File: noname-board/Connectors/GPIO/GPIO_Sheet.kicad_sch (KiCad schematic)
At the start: 1 part, among them J1 GPIO_CONNECTOR

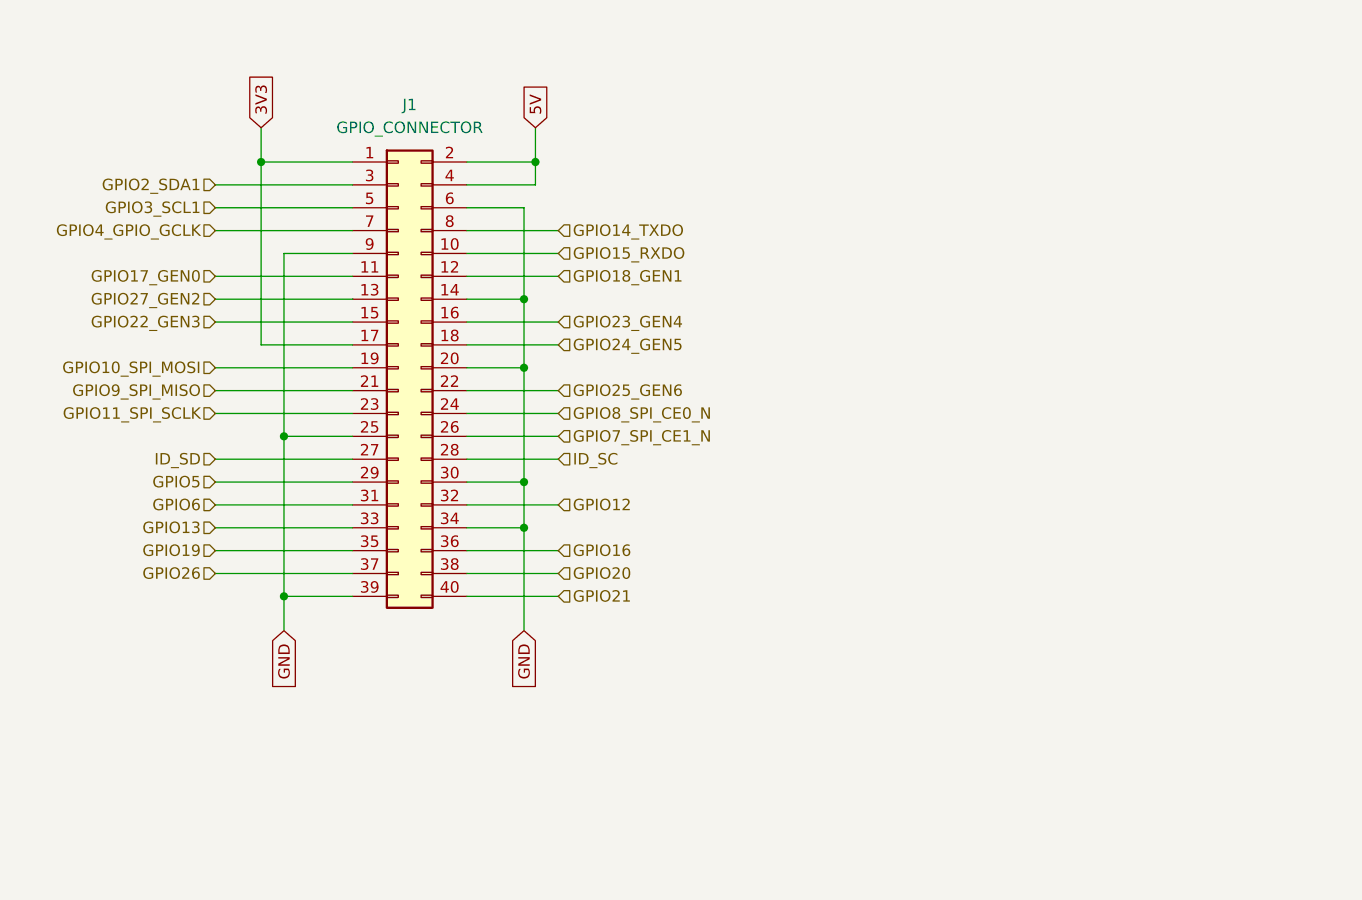
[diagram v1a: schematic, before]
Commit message: GPIO, USBC
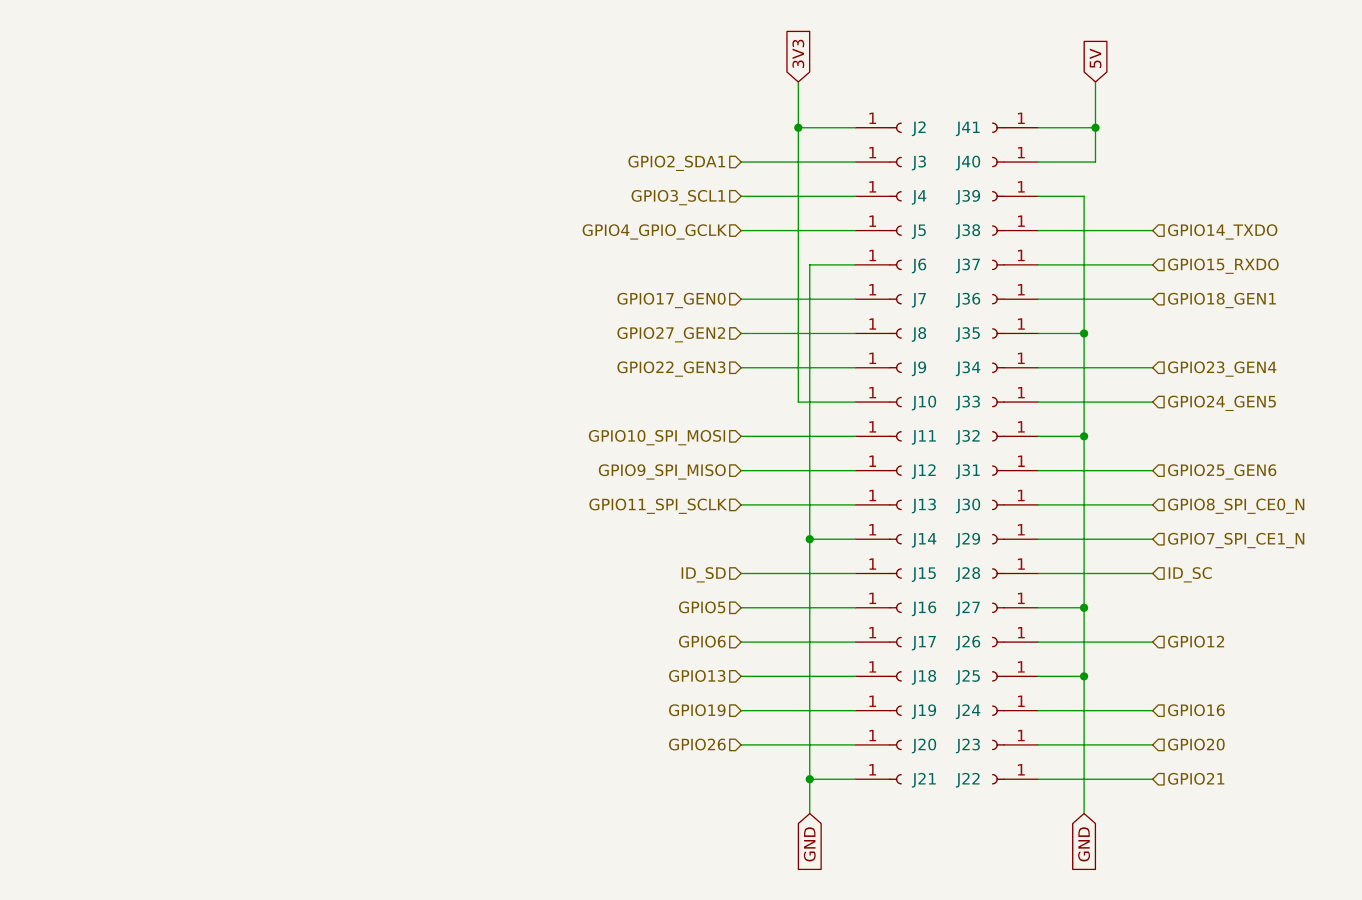
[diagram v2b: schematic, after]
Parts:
- removed J1: GPIO_CONNECTOR, symbol Connector_Generic:Conn_02x20_Odd_Even
- added J10, J11, J12, J13, J14, J15, J16, J17, J18, J19, J2, J20, J21, J22, J23, J24, J25, J26, J27, J28, J29, J3, J30, J31, J32, J33, J34, J35, J36, J37, J38, J39, J4, J40, J41, J5, J6, J7, J8, J9: Conn_01x01_Socket, Connector_PinSocket_2.00mm:PinSocket_1x01_P2.00mm_Vertical, symbol Connector:Conn_01x01_Socket
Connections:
- net 3V3: now also J10.1 (Pin_1), J2.1 (Pin_1)
- net 5V: now also J40.1 (Pin_1), J41.1 (Pin_1)
- net GND: now also J14.1 (Pin_1), J21.1 (Pin_1), J25.1 (Pin_1), J27.1 (Pin_1), J32.1 (Pin_1), J35.1 (Pin_1), J39.1 (Pin_1), J6.1 (Pin_1)
- net GPIO10_SPI_MOSI: now also J11.1 (Pin_1)
- net GPIO11_SPI_SCLK: now also J13.1 (Pin_1)
- net GPIO12: now also J26.1 (Pin_1)
- net GPIO13: now also J18.1 (Pin_1)
- net GPIO14_TXDO: now also J38.1 (Pin_1)
- net GPIO15_RXDO: now also J37.1 (Pin_1)
- net GPIO16: now also J24.1 (Pin_1)
- net GPIO17_GEN0: now also J7.1 (Pin_1)
- net GPIO18_GEN1: now also J36.1 (Pin_1)
- net GPIO19: now also J19.1 (Pin_1)
- net GPIO20: now also J23.1 (Pin_1)
- net GPIO21: now also J22.1 (Pin_1)
- net GPIO22_GEN3: now also J9.1 (Pin_1)
- net GPIO23_GEN4: now also J34.1 (Pin_1)
- net GPIO24_GEN5: now also J33.1 (Pin_1)
- net GPIO25_GEN6: now also J31.1 (Pin_1)
- net GPIO26: now also J20.1 (Pin_1)
- net GPIO27_GEN2: now also J8.1 (Pin_1)
- net GPIO2_SDA1: now also J3.1 (Pin_1)
- net GPIO3_SCL1: now also J4.1 (Pin_1)
- net GPIO4_GPIO_GCLK: now also J5.1 (Pin_1)
- net GPIO5: now also J16.1 (Pin_1)
- net GPIO6: now also J17.1 (Pin_1)
- net GPIO7_SPI_CE1_N: now also J29.1 (Pin_1)
- net GPIO8_SPI_CE0_N: now also J30.1 (Pin_1)
- net GPIO9_SPI_MISO: now also J12.1 (Pin_1)
- net ID_SC: now also J28.1 (Pin_1)
- net ID_SD: now also J15.1 (Pin_1)

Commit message: We went thru eveeeryyything
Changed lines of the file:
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@@
+    (stroke (width 0) (type default))
+  )
+  (wire (pts (xy 199.39 39.37) (xy 199.39 44.45))
     (stroke (width 0) (type default))
   )
@@
     (stroke (width 0) (type default))
   )
-  (wire (pts (xy 199.39 44.45) (xy 199.39 39.37))
-    (stroke (width 0) (type default))
-  )
   (wire (pts (xy 198.12 105.41) (xy 198.12 120.65))
     (stroke (width 0) (type default))
@@
     (stroke (width 0) (type default))
   )
-  (global_label "5V" (shape input) (at 199.39 39.37 90) (fields_autoplaced)
-    (effects (font (size 1.27 1.27)) (justify left))
-    (property "Intersheetrefs" "${INTERSHEET_REFS}" (at 199.39 34.0867 90)
-      (effects (font (size 1.27 1.27)) (justify left) hide)
-    )
-  )
-  (global_label "3V3" (shape input) (at 166.37 39.37 90) (fields_autoplaced)
-    (effects (font (size 1.27 1.27)) (justify left))
-    (property "Intersheetrefs" "${INTERSHEET_REFS}" (at 166.37 32.8772 90)
-      (effects (font (size 1.27 1.27)) (justify left) hide)
-    )
-  )
-  (global_label "GND" (shape input) (at 198.12 120.65 270) (fields_autoplaced)
-    (effects (font (size 1.27 1.27)) (justify right))
-    (property "Intersheetrefs" "${INTERSHEET_REFS}" (at 198.12 127.5057 90)
-      (effects (font (size 1.27 1.27)) (justify right) hide)
-    )
-  )
-  (global_label "GND" (shape input) (at 167.64 120.65 270) (fields_autoplaced)
-    (effects (font (size 1.27 1.27)) (justify right))
-    (property "Intersheetrefs" "${INTERSHEET_REFS}" (at 167.64 127.5057 90)
-      (effects (font (size 1.27 1.27)) (justify right) hide)
-    )
-  )
   (hierarchical_label "GPIO19" (shape input) (at 160.02 109.22 180) (fields_autoplaced)
     (effects (font (size 1.27 1.27)) (justify right))
   )
+  (hierarchical_label "GND" (shape input) (at 167.64 120.65 270) (fields_autoplaced)
+    (effects (font (size 1.27 1.27)) (justify right))
+  )
   (hierarchical_label "GPIO5" (shape input) (at 160.02 97.79 180) (fields_autoplaced)
+    (effects (font (size 1.27 1.27)) (justify right))
+  )
+  (hierarchical_label "GND" (shape input) (at 198.12 120.65 270) (fields_autoplaced)
     (effects (font (size 1.27 1.27)) (justify right))
   )
@@
     (effects (font (size 1.27 1.27)) (justify right))
   )
+  (hierarchical_label "5V" (shape input) (at 199.39 39.37 90) (fields_autoplaced)
+    (effects (font (size 1.27 1.27)) (justify left))
+  )
   (hierarchical_label "GPIO25_GEN6" (shape input) (at 205.74 82.55 0) (fields_autoplaced)
     (effects (font (size 1.27 1.27)) (justify left))
   )
+  (hierarchical_label "3V3" (shape input) (at 166.37 39.37 90) (fields_autoplaced)
+    (effects (font (size 1.27 1.27)) (justify left))
+  )
